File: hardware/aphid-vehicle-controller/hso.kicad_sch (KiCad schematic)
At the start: 3 parts, among them U8 BTS6143D

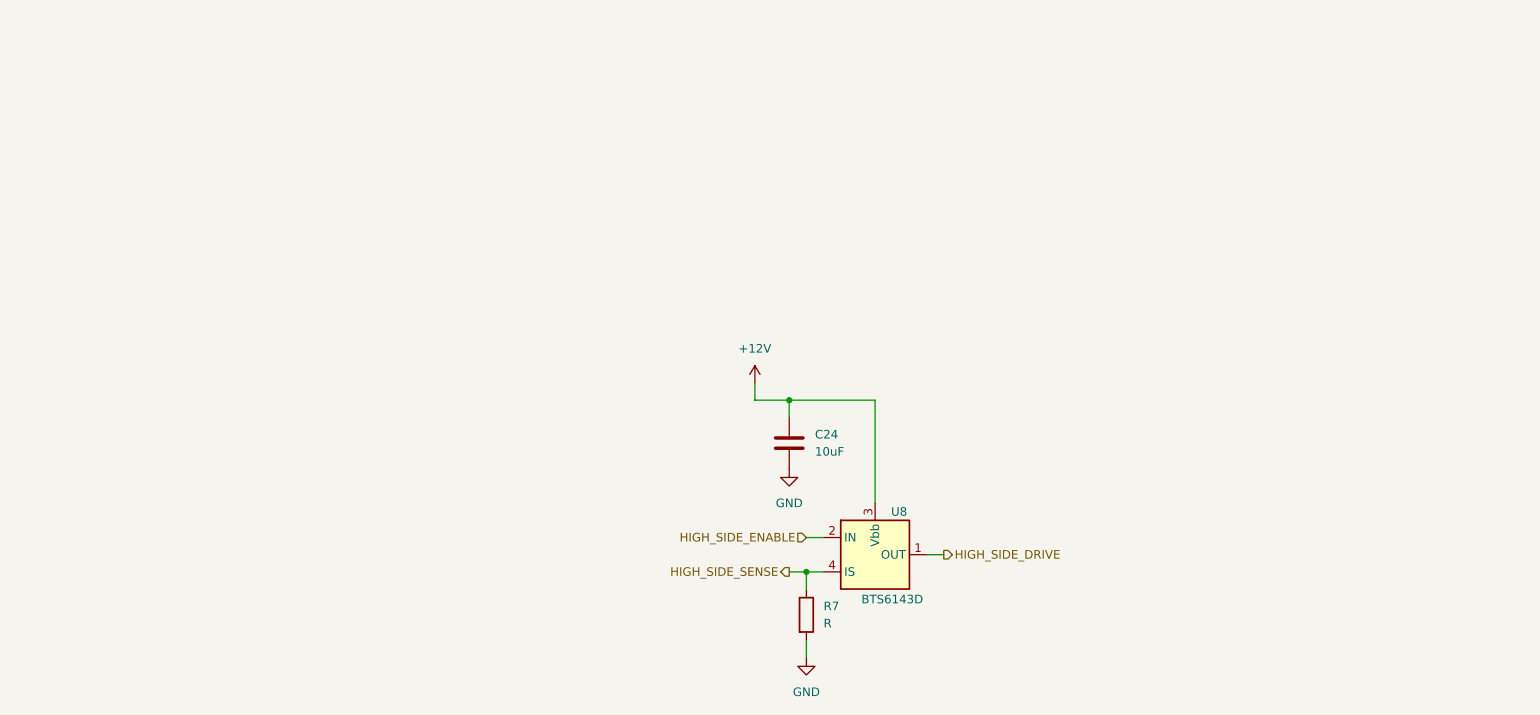
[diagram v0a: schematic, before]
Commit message: feat: changed to STM32G4xx series MCU
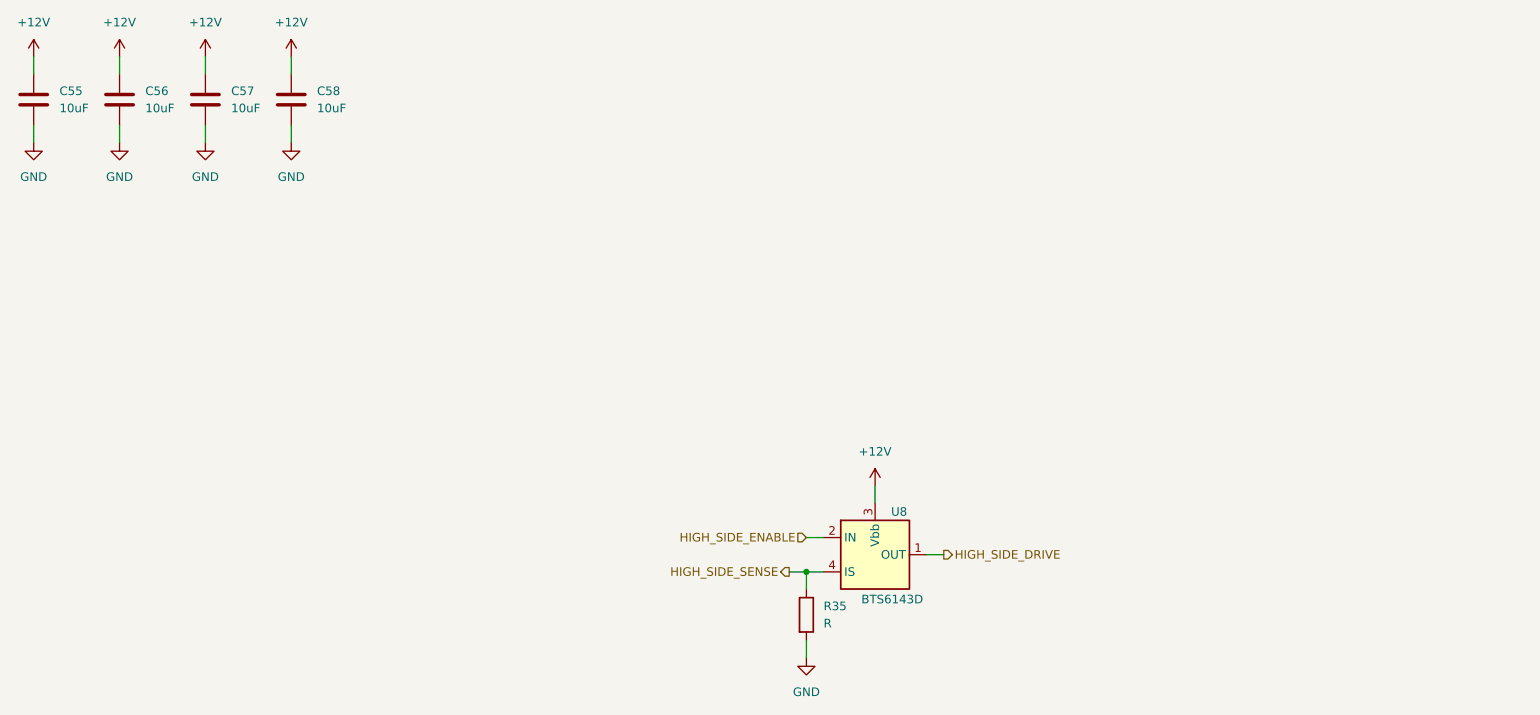
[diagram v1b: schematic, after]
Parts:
- added C55, C57, C58: 10uF, Capacitor_SMD:C_0805_2012Metric, symbol Device:C
- C56: renamed from C24; footprint (none) -> Capacitor_SMD:C_0805_2012Metric
- R35: renamed from R7; footprint (none) -> Resistor_SMD:R_0603_1608Metric
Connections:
- net +12V: now also C55.1, C57.1, C58.1
- net GND: now also C55.2, C57.2, C58.2
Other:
- moved on the sheet: C56

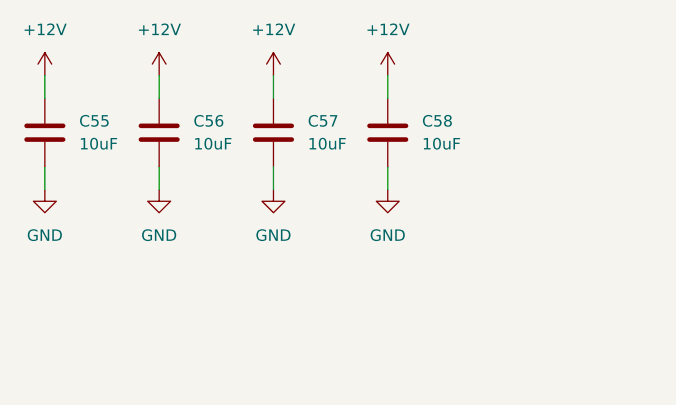
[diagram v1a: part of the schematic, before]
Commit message: feat: changed to a more modern DCDC
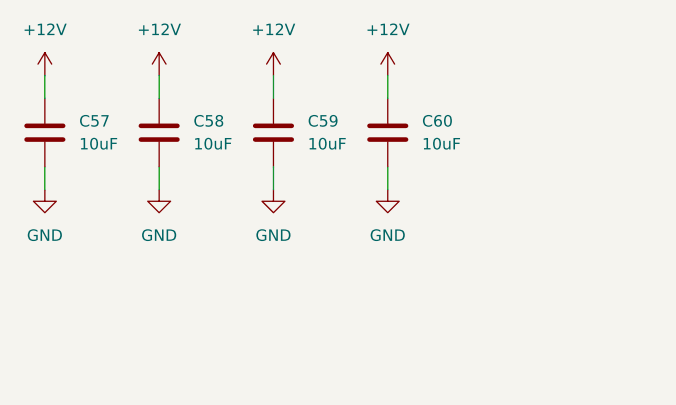
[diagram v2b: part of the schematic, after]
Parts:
- renumbered C55 to C57, C56 to C58, C57 to C59, C58 to C60
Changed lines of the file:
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@@
 		(dnp no)
 		(fields_autoplaced yes)
-		(property "Reference" "C55"
+		(property "Reference" "C57"
 			(at 29.21 30.4799 0)
 			(effects
@@
 			(project "aphid-vehicle-controller"
 				(path "/1bdad060-e59b-443f-afdb-9aa678a43546/3d287df9-d378-446a-9a45-9deed77b9c83"
-					(reference "C55")
+					(reference "C57")
 					(unit 1)
 				)
@@
 		(dnp no)
 		(fields_autoplaced yes)
-		(property "Reference" "C57"
+		(property "Reference" "C59"
 			(at 54.61 30.4799 0)
 			(effects
@@
 			(project "aphid-vehicle-controller"
 				(path "/1bdad060-e59b-443f-afdb-9aa678a43546/3d287df9-d378-446a-9a45-9deed77b9c83"
-					(reference "C57")
+					(reference "C59")
 					(unit 1)
 				)
@@
 		(dnp no)
 		(fields_autoplaced yes)
-		(property "Reference" "C58"
+		(property "Reference" "C60"
 			(at 67.31 30.4799 0)
 			(effects
@@
 			(project "aphid-vehicle-controller"
 				(path "/1bdad060-e59b-443f-afdb-9aa678a43546/3d287df9-d378-446a-9a45-9deed77b9c83"
-					(reference "C58")
+					(reference "C60")
 					(unit 1)
 				)
@@
 		(dnp no)
 		(fields_autoplaced yes)
-		(property "Reference" "C56"
+		(property "Reference" "C58"
 			(at 41.91 30.4799 0)
 			(effects
@@
 			(project "aphid-vehicle-controller"
 				(path "/1bdad060-e59b-443f-afdb-9aa678a43546/3d287df9-d378-446a-9a45-9deed77b9c83"
-					(reference "C56")
-					(unit 1)
-				)
+					(reference "C58")
+					(unit 1)
+				)

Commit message: Worked on VC PCB
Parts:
- C59: renamed from C57; value 10uF -> 10 uF 50V; footprint Capacitor_SMD:C_0805_2012Metric -> Capacitor_SMD:C_1206_3216Metric
- C60: renamed from C58; value 10uF -> 10 uF 50V; footprint Capacitor_SMD:C_0805_2012Metric -> Capacitor_SMD:C_1206_3216Metric
- C61: renamed from C59; value 10uF -> 10 uF 50V; footprint Capacitor_SMD:C_0805_2012Metric -> Capacitor_SMD:C_1206_3216Metric
- C62: renamed from C60; value 10uF -> 10 uF 50V; footprint Capacitor_SMD:C_0805_2012Metric -> Capacitor_SMD:C_1206_3216Metric
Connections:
- net +12V: no longer C59.1, C60.1, C61.1, C62.1
- net HIGH_SIDE_DRIVE: now also C59.1, C60.1, C61.1, C62.1
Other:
- moved on the sheet: C59, C60, C61, C62
